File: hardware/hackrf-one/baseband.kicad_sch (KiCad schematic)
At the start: 98 parts, among them P14 XCVR_CLKOUT, P39 SSP1_SCK, P40 SSP1_COPI, P41 SSP1_CIPO, P53 CS_XCVR, P54 CS_AD, P56 RXENABLE, P61 DA0, P62 DA7, P63 DD0, P64 DD9, P65 DA4, P66 DD5, P67 RSSI, P83 GND, P84 GND, P85 GND, P86 GND, P87 GND, P88 GND, P89 GND, P9 BASEBAND, P90 GND, P91 GND, P92 GND, Q3 MOSFET_P, T3 RX_BALUN, T4 TX_BALUN, U17 MAX2839, U18 MAX5864

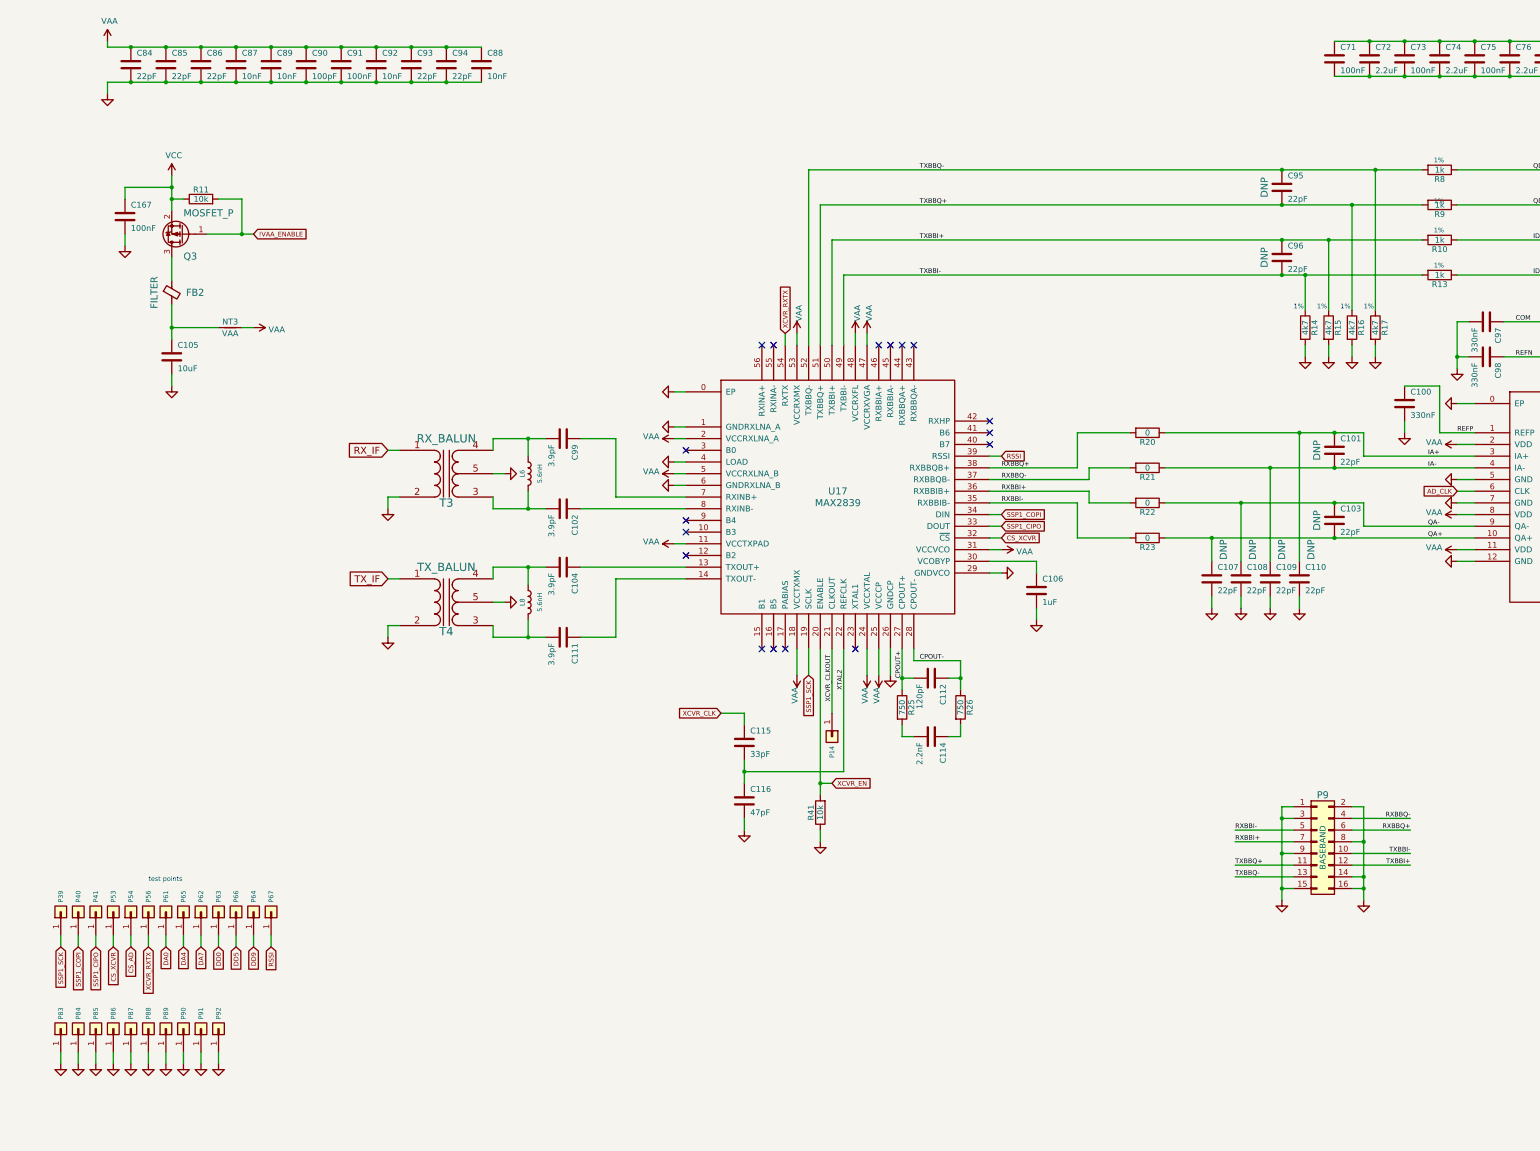
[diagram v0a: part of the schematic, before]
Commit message: HackRF One: revert hardware design to 8727449
This commit is between r8 and r9 and will be used as the basis for r10.
It includes some of the changes in r9 but predates the major changes to
the clock generator and IF transceiver ICs.
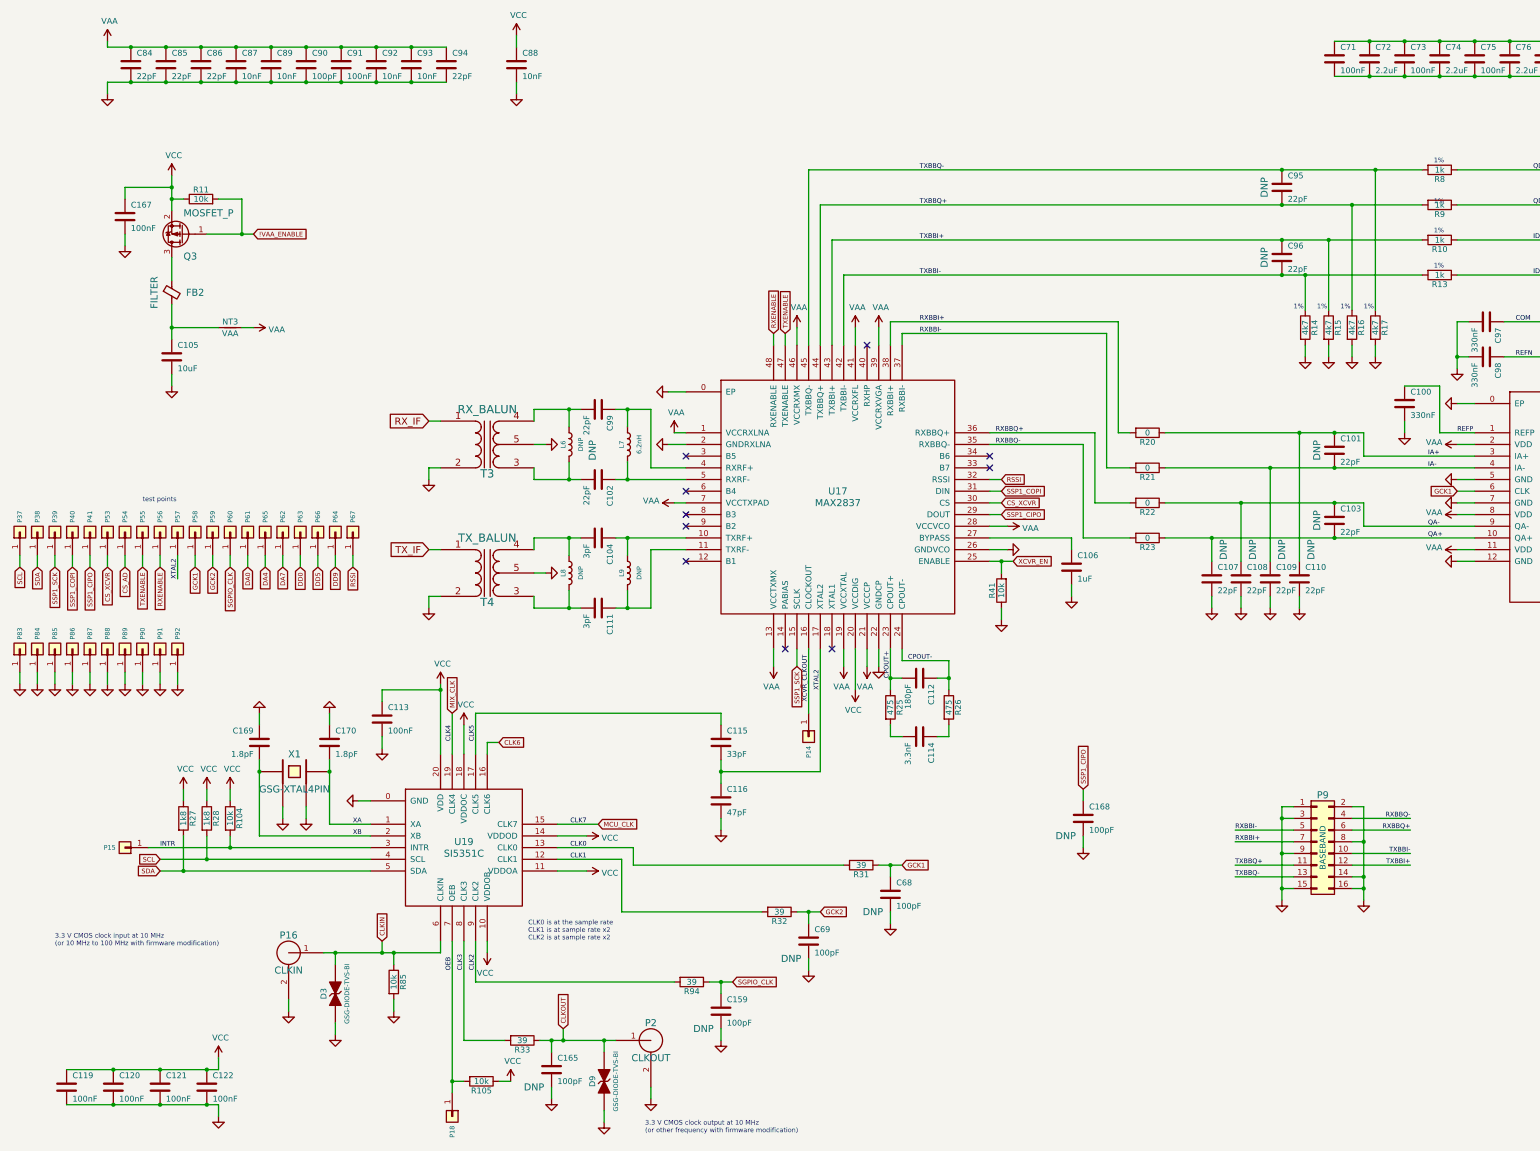
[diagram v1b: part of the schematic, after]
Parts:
- added C113, C119, C120, C121, C122: 100nF, hackrf:GSG-0402, symbol Device:C
- added C159, C165, C168, C68, C69: 100pF, hackrf:GSG-0402, symbol Device:C
- added C169, C170: 1.8pF, hackrf:GSG-0402, symbol Device:C
- added D3, D9: GSG-DIODE-TVS-BI, hackrf:GSG-0402, symbol hackrf:GSG-DIODE-TVS-BI
- added L7: 6.2nH, hackrf:GSG-0402, symbol Device:L
- added L9: DNP, hackrf:GSG-0402, symbol Device:L
- added P15: INTR, hackrf:GSG-TESTPOINT-50MIL, symbol Connector_Generic:Conn_01x01
- added P16: CLKIN, hackrf:GSG-SMA-73251-2120, symbol hackrf:GSG-RF-CONN
- added P18: OEB, hackrf:GSG-TESTPOINT-50MIL, symbol Connector_Generic:Conn_01x01
- added P2: CLKOUT, hackrf:GSG-SMA-73251-2120, symbol hackrf:GSG-RF-CONN
- added P37: SCL, hackrf:GSG-TESTPOINT-50MIL, symbol Connector_Generic:Conn_01x01
- added P38: SDA, hackrf:GSG-TESTPOINT-50MIL, symbol Connector_Generic:Conn_01x01
- added P55: TXENABLE, hackrf:GSG-TESTPOINT-50MIL, symbol Connector_Generic:Conn_01x01
- added P57: XTAL2, hackrf:GSG-TESTPOINT-50MIL, symbol Connector_Generic:Conn_01x01
- added P58: GCK1, hackrf:GSG-TESTPOINT-50MIL, symbol Connector_Generic:Conn_01x01
- added P59: GCK2, hackrf:GSG-TESTPOINT-50MIL, symbol Connector_Generic:Conn_01x01
- added P60: SGPIO_CLK, hackrf:GSG-TESTPOINT-50MIL, symbol Connector_Generic:Conn_01x01
- added R104, R105, R85: 10k, hackrf:GSG-0402, symbol Device:R
- added R27, R28: 1k8, hackrf:GSG-0402, symbol Device:R
- added R31, R32, R33, R94: 39, hackrf:GSG-0402, symbol Device:R
- added U19: SI5351C, hackrf:GSG-QFN20-4, symbol hackrf:SI5351C
- added X1: GSG-XTAL4PIN, hackrf:GSG-XTAL3.2x2.5mm, symbol hackrf:GSG-XTAL4PIN
- C100, C97, C98: Manufacturer Yageo -> Murata; Part Number CC0402KRX5R6BB334 -> GRM155R61A334KE15D
- C101, C103, C107, C108, C109, C110, C95, C96: DNP DNP -> (none); Manufacturer Samsung -> Murata; Note (none) -> DNP; Part Number CL05C220JB5NNNC -> GRM1555C1H220JA01D
- C102, C99: value 3.9pF -> 22pF; Part Number GCM1555C1H3R9BA16D -> GRM1555C1H220JA01D
- C104, C111: value 3.9pF -> 3pF; Part Number GCM1555C1H3R9BA16D -> GRM1555C1H3R0CA01D
- C105: Manufacturer Samsung -> Murata; Part Number CL21A106KOQNNNE -> GRM21BR61A106KE19L
- C106: Manufacturer Samsung -> Taiyo Yuden; Part Number CL05A105KP5NNNC -> LMK105BJ105KV-F
- C112: value 120pF -> 180pF; Part Number GCM1555C1H121JA16D -> GRM1555C1H181JA01D
- C114: value 2.2nF -> 3.3nF; Part Number GRM155R71H222KA01D -> GRM155R71H332KA01D
- C115: Manufacturer Samsung -> Murata; Part Number CL05C330JB5NNNC -> GRM1555C1H330JA01D
- C116: Manufacturer Samsung -> Murata; Part Number CL05C470JB5NNNC -> GRM1555C1H470JA01D
- C123, C167, C71, C73, C75, C77, C79, C81, C83, C91: Manufacturer Samsung -> Murata; Part Number CL05A104KA5NNNC -> GRM155R61A104KA01D
- C84, C85, C86, C94: Manufacturer Samsung -> Murata; Part Number CL05C220JB5NNNC -> GRM1555C1H220JA01D
- C87, C88, C89, C92: Manufacturer Samsung -> Murata; Part Number CL05B103KB5NNNC -> GRM155R71C103KA01D
- C90: Manufacturer Samsung -> Murata; Part Number CL05C101JB5NNNC -> GRM1555C1H101JA01D
- C93: value 22pF -> 10nF; Manufacturer Samsung -> Murata; Part Number CL05C220JB5NNNC -> GRM155R71C103KA01D
- L6, L8: value 5.6nH -> DNP; Manufacturer Murata -> (none); Note (none) -> DNP; Part Number LQG15HS5N6S02D -> (none)
- NT3, P14, P39, P40, P41, P53, P54, P56, P61, P62, P63, P64, P65, P66, P67, P83, P84, P85, P86, P87, P88, P89, P90, P91, P92: DNP DNP -> (none); Note (none) -> DNP
- Q3: Manufacturer Yangzhou Yangjie -> Diodes Inc.; Part Number YJL2301C -> DMP2305U-7
- R25, R26: value 750 -> 475; Manufacturer Yageo -> Stackpole; Part Number RC0402FR-07750RL -> RMCF0402JT470R
- T3: Note Alternative part: Murata LDB182G4510G-120 -> (none); Note: (none) -> Alternative part: Murata LDB182G4510G-120
- U17: value MAX2839 -> MAX2837; footprint gsg-modules:QFN-56-1EP_8x8mm_P0.5mm_EP6.5x6.5mm_ThermalVias -> hackrf:GSG-QFN48-6; symbol hackrf:MAX2839 -> hackrf:MAX2837; Part Number MAX2839ETN+ -> MAX2837ETM+
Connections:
- net CPOUT+: now also U17.23 (CPOUT+); no longer U17.27 (CPOUT+)
- net CPOUT-: now also U17.24 (CPOUT-); no longer U17.28 (CPOUT-)
- net CS_XCVR: now also U17.30 (CS); no longer U17.32 (~{CS})
- net GND: now also U17.2 (GNDRXLNA), U17.22 (GNDCP), C113.2, C119.2, C120.2, C121.2, C122.2, C159.2, C165.2, C168.2, C169.1, C170.1, C68.2, C69.2, D3.1 (A), D9.1 (A), P16.2 (GND), P2.2 (GND), R85.2, U19.0 (GND), X1.2, X1.4; no longer U17.1 (GNDRXLNA_A), U17.29 (GNDVCO), U17.4 (LOAD), U17.6 (GNDRXLNA_B)
- net RSSI: now also U17.32 (RSSI); no longer U17.39 (RSSI)
- net RXBBI+: now also R20.2, U17.38 (RXBBI+); no longer R22.2, U17.36 (RXBBIB+)
- net RXBBI-: now also R21.2, U17.37 (RXBBI-); no longer R23.2, U17.35 (RXBBIB-)
- net RXBBQ+: now also R22.2, U17.36 (RXBBQ+); no longer R20.2, U17.38 (RXBBQB+)
- net RXBBQ-: now also R23.2, U17.35 (RXBBQ-); no longer R21.2, U17.37 (RXBBQB-)
- net SSP1_CIPO: now also U17.29 (DOUT), C168.1; no longer U17.33 (DOUT)
- net SSP1_COPI: now also U17.31 (DIN); no longer U17.34 (DIN)
- net SSP1_SCK: now also U17.15 (SCLK); no longer U17.19 (SCLK)
- net TXBBI+: now also U17.43 (TXBBI+); no longer U17.50 (TXBBI+)
- net TXBBI-: now also U17.42 (TXBBI-); no longer U17.49 (TXBBI-)
- net TXBBQ+: now also U17.44 (TXBBQ+); no longer U17.51 (TXBBQ+)
- net TXBBQ-: now also U17.45 (TXBBQ-); no longer U17.52 (TXBBQ-)
- net VAA: now also U17.1 (VCCRXLNA), U17.13 (VCCTXMX), U17.19 (VCCXTAL), U17.21 (VCCCP), U17.28 (VCCVCO), U17.39 (VCCRXVGA), U17.41 (VCCRXFL), U17.46 (VCCRXMX), U17.7 (VCCTXPAD); no longer C88.1, U17.11 (VCCTXPAD), U17.18 (VCCTXMX), U17.2 (VCCRXLNA_A), U17.24 (VCCXTAL), U17.25 (VCCCP), U17.31 (VCCVCO), U17.47 (VCCRXVGA), U17.48 (VCCRXFL), U17.5 (VCCRXLNA_B), U17.53 (VCCRXMX)
- net VCC: now also C88.1, U17.20 (VCCDIG), C113.1, C119.1, C120.1, C121.1, C122.1, R104.1, R105.1, R27.1, R28.1, U19.10 (VDDOB), U19.11 (VDDOA), U19.14 (VDDOD), U19.18 (VDDOC), U19.20 (VDD)
- net XCVR_CLKOUT: now also U17.16 (CLOCKOUT); no longer U17.21 (CLKOUT)
- net XCVR_EN: now also U17.25 (ENABLE); no longer U17.20 (ENABLE)
- net XTAL2: now also U17.17 (XTAL2), P57.1 (Pin_1); no longer U17.22 (REFCLK)
- net at U17.10 (TXRF+): now also C104.1, L9.1
- net at C111.1: now also U17.11 (TXRF-), L9.2; no longer U17.14 (TXOUT-)
- net at C106.1: now also U17.27 (BYPASS); no longer U17.30 (VCOBYP)
- net at C99.1: now also U17.4 (RXRF+), L7.1; no longer U17.7 (RXINB+)
- net at C102.1: now also U17.5 (RXRF-), L7.2; no longer U17.8 (RXINB-)
- net AD_CLK renamed GCK1
- net GCK1: now also C68.1, P58.1 (Pin_1), R31.1
- net XCVR_CLK renamed CLK5
- net CLK5: now also U19.17 (CLK5)
- net XCVR_RXTX renamed RXENABLE
- net RXENABLE: now also U17.48 (RXENABLE); no longer U17.54 (RXTX)
- new net CLK0: R31.2, U19.13 (CLK0)
- new net CLK1: R32.2, U19.12 (CLK1)
- new net CLK2: R94.2, U19.9 (CLK2)
- new net CLK3: R33.2, U19.8 (CLK3)
- new net CLK6: U19.16 (CLK6)
- new net CLKIN: D3.2 (K), P16.1 (RF), R85.1, U19.6 (CLKIN)
- new net CLKOUT: C165.1, D9.2 (K), P2.1 (RF), R33.1
- new net GCK2: C69.1, P59.1 (Pin_1), R32.1
- new net INTR: P15.1 (Pin_1), R104.2, U19.3 (INTR)
- new net MCU_CLK: U19.15 (CLK7)
- new net MIX_CLK: U19.19 (CLK4)
- new net OEB: P18.1 (Pin_1), R105.2, U19.7 (OEB)
- new net SCL: P37.1 (Pin_1), R28.2, U19.4 (SCL)
- new net SDA: P38.1 (Pin_1), R27.2, U19.5 (SDA)
- new net SGPIO_CLK: C159.1, P60.1 (Pin_1), R94.1
- new net TXENABLE: P55.1 (Pin_1), U17.47 (TXENABLE)
- new net XA: C170.2, U19.1 (XA), X1.3
- new net XB: C169.2, U19.2 (XB), X1.1
- no-connect marks 17 -> 10
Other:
- note added: "3.3 V CMOS clock input at 10 MHz (or 10 MHz to 100 MHz with firmware modification)"
- note added: "3.3 V CMOS clock output at 10 MHz (or other frequency with firmware modification)"
- note added: "CLK0 is at the sample rate CLK1 is at sample rate x2 CLK2 is at sample rate x2"
- moved on the sheet: C102, C104, C106, C111, C112, C114, C115, C116, C88, C99, L6, L8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

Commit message: HackRF One: update version to 8+
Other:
- company: Copyright 2012-2022 Great Scott Gadgets -> ${COPYRIGHT}
- title: HackRF One -> ${TITLE}
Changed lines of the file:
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@@
   (paper "User" 431.8 279.4)
   (title_block
-    (title "HackRF One")
-    (date "2022-08-28")
-    (rev "r9")
-    (company "Copyright 2012-2022 Great Scott Gadgets")
-    (comment 1 "Michael Ossmann")
-    (comment 2 "Licensed under the CERN-OHL-P v2")
+    (title "${TITLE}")
+    (date "${DATE}")
+    (rev "${VERSION}")
+    (company "${COPYRIGHT}")
+    (comment 1 "${LICENSE}")
   )
   (junction (at 80.01 27.94) (diameter 0) (color 0 0 0 0)

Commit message: HackRF One: use DNP field instead of Note field
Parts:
- C101, C103, C107, C108, C109, C110, C159, C165, C168, C68, C69, C95, C96, L6, L8, L9, NT3, P14, P15, P18, P37, P38, P39, P40, P41, P53, P54, P55, P56, P57, P58, P59, P60, P61, P62, P63, P64, P65, P66, P67, P83, P84, P85, P86, P87, P88, P89, P90, P91, P92: DNP (none) -> DNP; Note DNP -> (none)
- T3: Note (none) -> Alternative part: Murata LDB182G4510G-120; Note: Alternative part: Murata LDB182G4510G-120 -> (none)

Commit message: HackRF One: update component selections
Add Substitution field
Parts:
- C100, C97, C98: Manufacturer Murata -> Yageo; Part Number GRM155R61A334KE15D -> CC0402KRX5R6BB334; Substitution (none) -> Murata GRM155R61A334KE15D
- C101, C102, C103, C107, C108, C109, C110, C84, C85, C86, C94, C95, C96, C99: Manufacturer Murata -> Samsung; Part Number GRM1555C1H220JA01D -> CL05C220JB5NNNC; Substitution (none) -> Murata GRM1555C1H220JA01D
- C104, C111: Part Number GRM1555C1H3R0CA01D -> GCM1555C1H3R0CA16D
- C105: Manufacturer Murata -> Samsung; Part Number GRM21BR61A106KE19L -> CL21A106KOQNNNE; Substitution (none) -> Murata GRM21BR61A106KE19L
- C106: Manufacturer Taiyo Yuden -> Samsung; Part Number LMK105BJ105KV-F -> CL05A105KP5NNNC; Substitution (none) -> Taiyo Yuden LMK105BJ105KV-F
- C112: Manufacturer Murata -> Yageo; Part Number GRM1555C1H181JA01D -> CC0402JRNPO9BN181; Substitution (none) -> Murata GRM1555C1H181JA01D
- C114: Manufacturer Murata -> Yageo; Part Number GRM155R71H332KA01D -> CC0402KRX7R9BB332
- C115: Manufacturer Murata -> Samsung; Part Number GRM1555C1H330JA01D -> CL05C330JB5NNNC; Substitution (none) -> Murata GRM1555C1H330JA01D
- C116: Manufacturer Murata -> Samsung; Part Number GRM1555C1H470JA01D -> CL05C470JB5NNNC; Substitution (none) -> Murata GRM1555C1H470JA01D
- C159, C165, C168, C68, C69, C90: Manufacturer Murata -> Samsung; Part Number GRM1555C1H101JA01D -> CL05C101JB5NNNC; Substitution (none) -> Murata GRM1555C1H101JA01D
- C169, C170: Manufacturer Murata -> Yageo; Part Number GRM1555C1E1R8BA01D -> CC0402CRNPO9BN1R8
- C87, C88, C89, C92, C93: Manufacturer Murata -> Samsung; Part Number GRM155R71C103KA01D -> CL05B103KB5NNNC; Substitution (none) -> Murata GRM155R71C103KA01D
- L7: Manufacturer Taiyo Yuden -> Murata; Part Number HK10056N2S-T -> LQG15HS6N2S02D; Substitution (none) -> Taiyo Yuden HK10056N2S-T
- Q3: Manufacturer Diodes Inc. -> Yangzhou Yangjie; Part Number DMP2305U-7 -> YJL2301C
- R10, R104, R105, R11, R13, R14, R15, R16, R17, R20, R21, R22, R23, R25, R26, R27, R28, R31, R32, R33, R41, R8, R85, R9, R94: Substitution (none) -> any equivalent
- T3, T4: Note Alternative part: Murata LDB182G4510G-120 -> (none); Substitution (none) -> Murata LDB182G4510G-120
- U17: Part Number MAX2837ETM+ -> MAX2837ETM+T; Substitution (none) -> MAX2837ETM+
- U18: Part Number MAX5864ETM+ -> MAX5864ETM+T; Substitution (none) -> MAX5864ETM+

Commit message: HackRF One: update 100 nF capacitor part selection
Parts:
- C113, C119, C120, C121, C122, C123, C167, C71, C73, C75, C77, C79, C81, C83, C91: Manufacturer Murata -> Samsung; Part Number GRM155R61A104KA01D -> CL05A104KA5NNNC; Substitution (none) -> Murata GRM155R61A104KA01D
